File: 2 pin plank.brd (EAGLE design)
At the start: 80 x 49 mm, 4 parts, among them IC1 74AHC1G86DBV

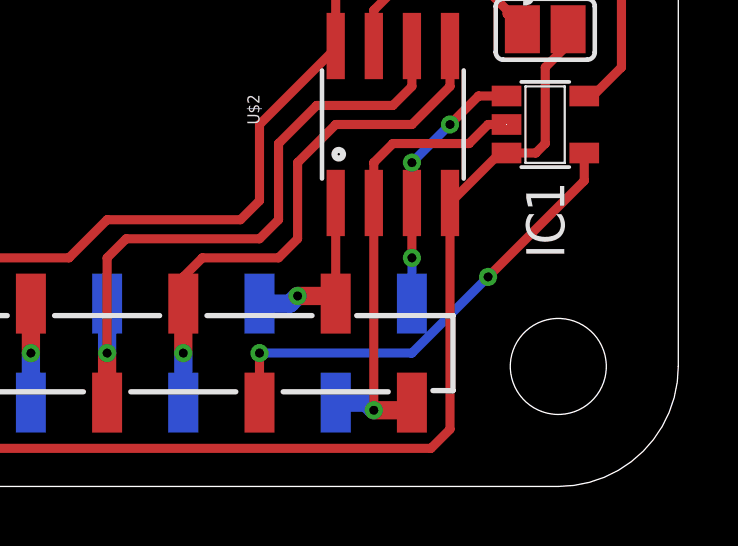
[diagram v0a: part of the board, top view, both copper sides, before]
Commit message: Minor layout changes; improvements to 2 pin plank template.
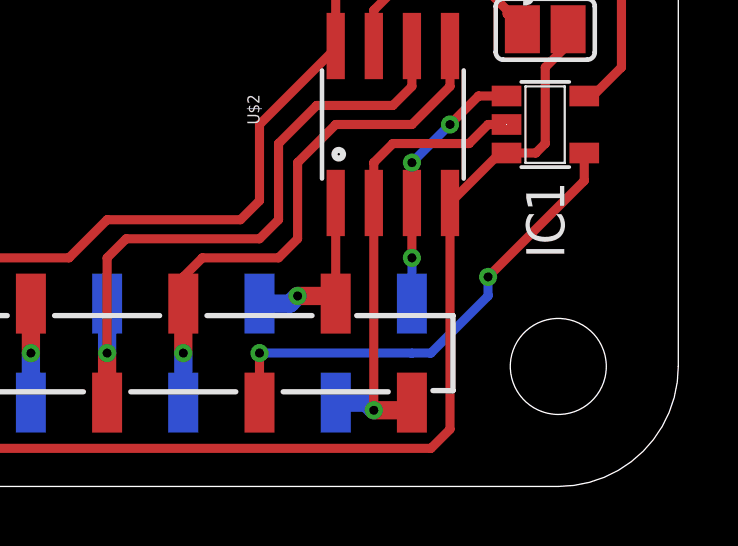
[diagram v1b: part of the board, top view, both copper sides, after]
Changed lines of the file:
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@@
 <wire x1="78.135" y1="10.19" x2="74.93" y2="6.985" width="0.3048" layer="1"/>
 <via x="74.93" y="6.985" extent="1-16" drill="0.3"/>
-<wire x1="74.93" y1="6.985" x2="72.39" y2="4.445" width="0.3048" layer="16"/>
 <wire x1="72.39" y1="4.445" x2="67.31" y2="4.445" width="0.3048" layer="16"/>
 <via x="67.31" y="4.445" extent="1-16" drill="0.3"/>
 <wire x1="67.31" y1="4.445" x2="67.31" y2="2.795" width="0.3048" layer="1"/>
+<wire x1="72.39" y1="4.445" x2="73.025" y2="4.445" width="0.3048" layer="16"/>
+<wire x1="73.025" y1="4.445" x2="74.93" y2="6.35" width="0.3048" layer="16"/>
+<wire x1="74.93" y1="6.35" x2="74.93" y2="6.985" width="0.3048" layer="16"/>
 </signal>
 <signal name="SCL">
